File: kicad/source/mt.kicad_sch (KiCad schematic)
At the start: 18 parts, among them IC1 MSPM0G3507SPMR, IC2 DAC082S085CIMMX_NOPB, IC3 IS62WV1288BLL-55QLI, IC4 MCP73831T-2ACI_OT, IC5 RT9167A-33GB, IC6 SN74HC148NSR, IC7 TLV9152IDR, IC8 TPS613222ADBVR, IC9 BQ29728DSER, J1 694106301002, J2 SJ1-3524N, Q1 CSD16406Q3, Q2 CSD16406Q3, U1 1043

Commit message: completed power electronics schematic
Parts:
- removed VR2: PTV09A-4020F-C103, PTV09A-4020F-C103:PTV09A4020FC103, symbol PTV09A-4020F-C103:PTV09A-4020F-C103
- added C1, C2, C4, C7: 4.7u, Capacitor_SMD:C_0402_1005Metric, symbol Device:C
- added C3, C8: 0.1u, Capacitor_SMD:C_0402_1005Metric, symbol Device:C
- added C5, C6: 22u, Capacitor_SMD:C_0603_1608Metric, symbol Device:C
- added D1: LED, LED_THT:LED_D5.0mm, symbol Device:LED
- added J3: Conn_01x05_MountingPin, Connector_PinHeader_2.54mm:PinHeader_1x05_P2.54mm_Horizontal, symbol Connector_Generic_MountingPin:Conn_01x05_MountingPin
- added L1: 2.2u, Inductor_SMD:L_1008_2520Metric, symbol Device:L
- added R1: 4.7k, Resistor_SMD:R_0402_1005Metric, symbol Device:R_US
- added R2: 2k, Resistor_SMD:R_0402_1005Metric, symbol Device:R_US
- added R3: 2.2k, Resistor_SMD:R_0402_1005Metric, symbol Device:R_US
- added R4: 330, Resistor_SMD:R_0402_1005Metric, symbol Device:R_US
- added VR2: PTV112-4420A-C104, PTV1124420AC104, symbol PTV112-4420A-C104:PTV112-4420A-C104
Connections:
- net GND: now reaches Q1.1 (S_1), Q1.2 (S_2), Q1.3 (S_3)
- net GND: now also IC4.2 (VSS), IC5.2 (GND), IC8.2 (GND), J1.2 (GND_1), J1.3 (GND_2), C1.2, C2.2, C4.2, C5.2, C6.2, C7.2, C8.2, R2.2, R3.1
- net at Q1.4 (G): now also IC9.2 (COUT)
- net at Q1.5 (D_1), Q1.6 (D_2), Q1.7 (D_3)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: now also Q2.5 (D_1), Q2.6 (D_2), Q2.7 (D_3), Q2.8 (D_4)
- net at IC8.1 (SW): now also L1.1
- net at IC8.4 (VOUT): now also IC5.1 (VIN), IC5.3 (EN), C5.1, C6.1
- net at IC9.3 (DOUT): now also Q2.4 (G)
- net at IC9.4 (VSS): now also Q2.1 (S_1), Q2.2 (S_2), Q2.3 (S_3), U1.2 (-), C3.2
- net at IC9.5 (BAT): now also C3.1, R4.2
- net at IC9.6 (V-): now also R3.2
- net at J1.1 (POWER): now also IC4.4 (VDD), C1.1, D1.2 (A)
- net VBAT: now reaches S1.2
- net VBAT: now also C4.1, L1.2
- net CELL+: now reaches S1.3
- net CELL+: now also IC4.3 (VBAT), U1.1 (+), C2.1, R4.1
- net at IC4.1 (STAT): now also R1.2
- net at IC4.5 (PROG): now also R2.1
- net at IC5.4 (BP): now also C8.1
- net at IC5.5 (VOUT): now also C7.1
- net at S2.1: now also S2.2
- net at S2.3: now also S2.4
- new net: D1.1 (K), R1.1
- no-connect marks 5 -> 9
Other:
- note added: "Charging"
- note added: "Power"
- note added: "Protection"
- note added: "Regulation"
- note added: "TODO: add all JLCPCB part # to ICs!"
- moved on the sheet: IC4, IC5, IC8, IC9, J1, Q1, Q2, S1, U1

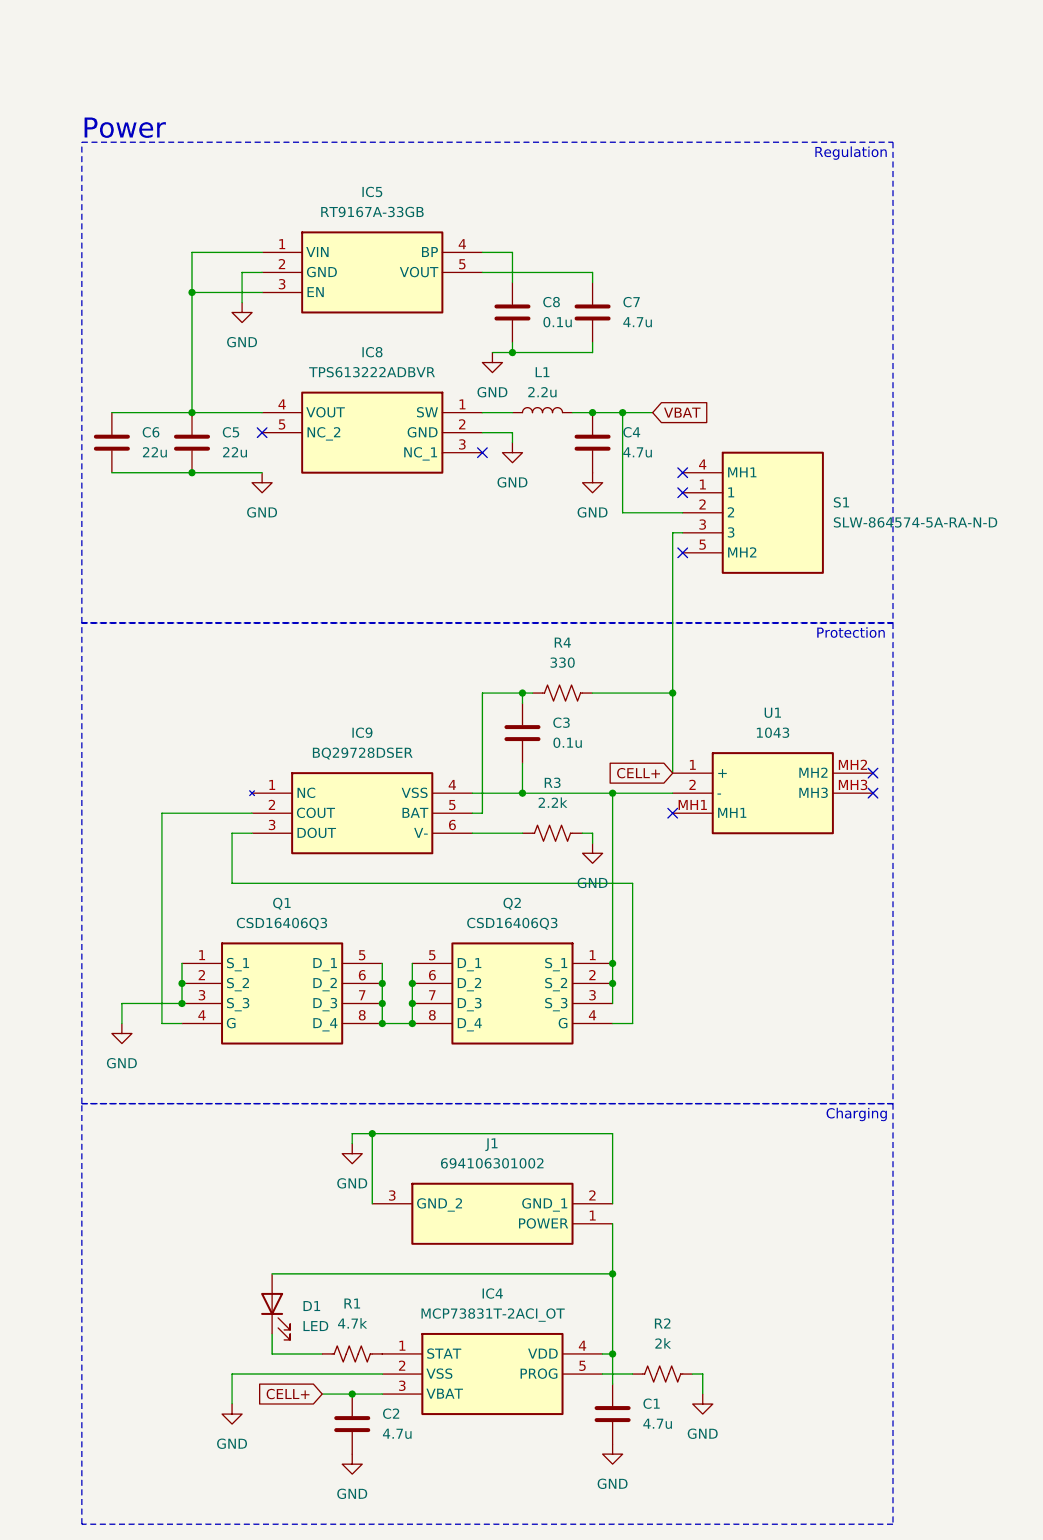
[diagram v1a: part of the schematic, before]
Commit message: revised power electronics caps, added JLCPCB part numbers to SMD power electronics
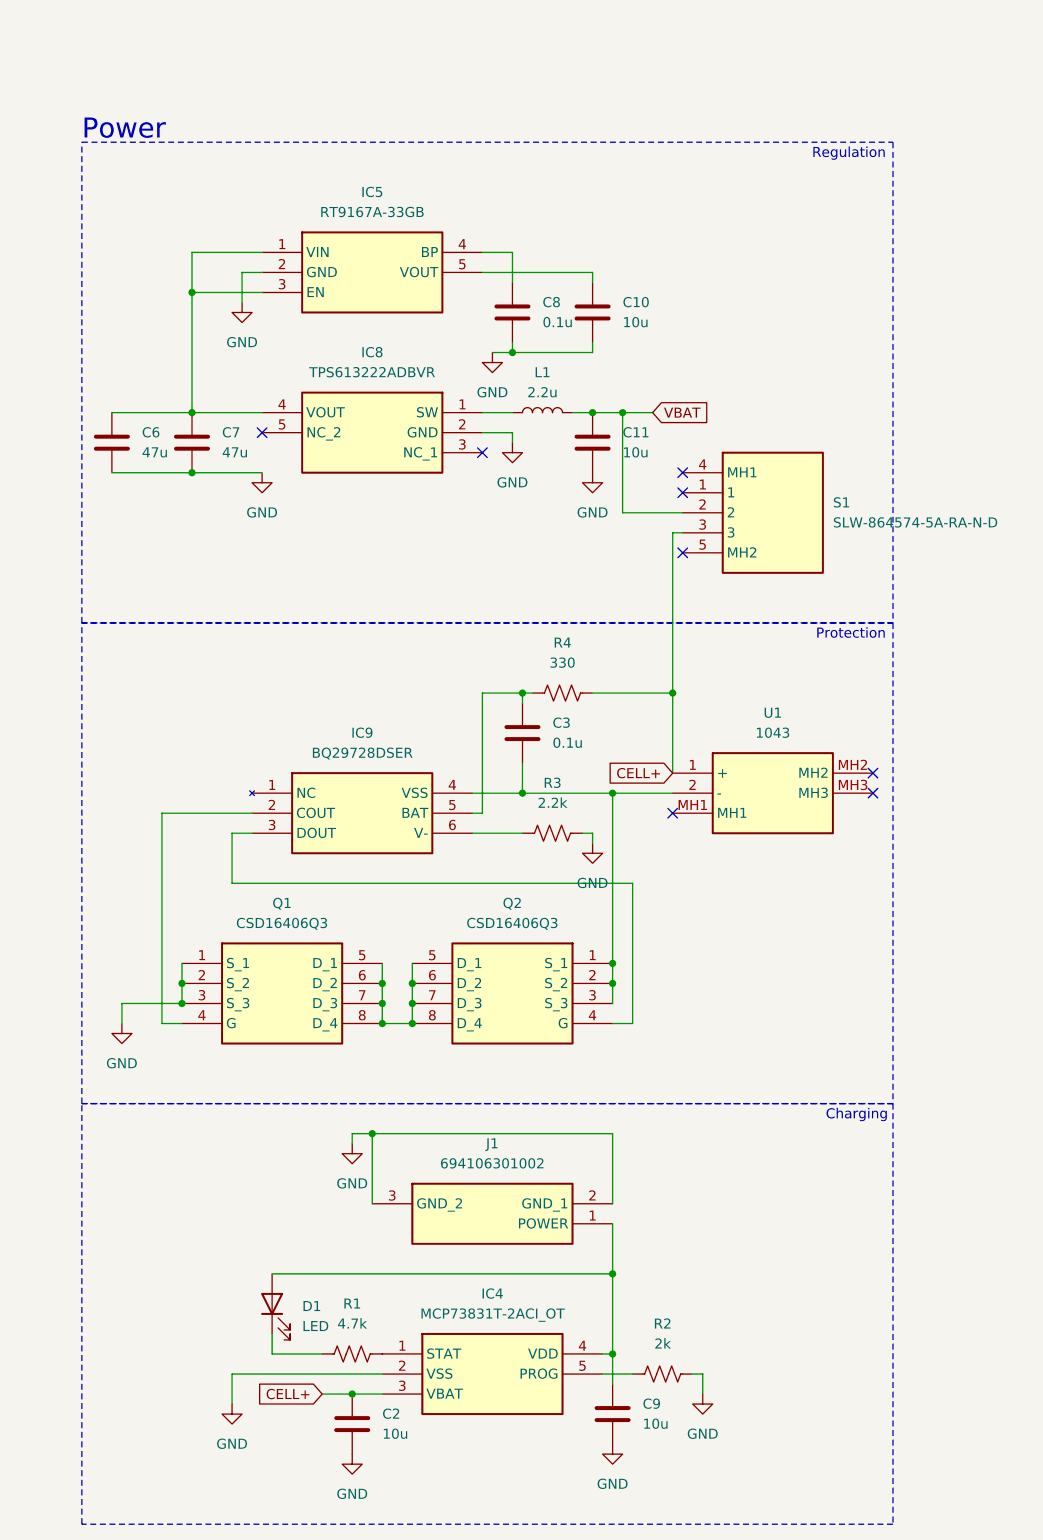
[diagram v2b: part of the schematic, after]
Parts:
- removed C1, C4: 4.7u, Capacitor_SMD:C_0402_1005Metric, symbol Device:C
- removed C5: 22u, Capacitor_SMD:C_0603_1608Metric, symbol Device:C
- added C10, C11, C9: 10u, Capacitor_SMD:C_0603_1608Metric, symbol Device:C
- C2: value 4.7u -> 10u; footprint Capacitor_SMD:C_0402_1005Metric -> Capacitor_SMD:C_0603_1608Metric; JLCPCB C23733 -> C19702
- C3, C8: footprint Capacitor_SMD:C_0402_1005Metric -> Capacitor_SMD:C_1206_3216Metric; JLCPCB C1525 -> C97946
- C6: value 22u -> 47u; footprint Capacitor_SMD:C_0603_1608Metric -> Capacitor_SMD:C_0805_2012Metric; JLCPCB C59461 -> C16780
- C7: value 4.7u -> 47u; footprint Capacitor_SMD:C_0402_1005Metric -> Capacitor_SMD:C_0805_2012Metric; JLCPCB C23733 -> C16780
- IC4: JLCPCB (none) -> C424093
- IC5: JLCPCB (none) -> C113513
- IC8: JLCPCB (none) -> C2071163
- IC9: JLCPCB (none) -> C3682679
- Q1, Q2: JLCPCB (none) -> C2861720
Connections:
- net GND: now also C10.2, C11.2, C9.2
- net VBAT: now also C11.1
- net at C7.1: now also C6.1, IC5.1 (VIN), IC5.3 (EN), IC8.4 (VOUT); no longer IC5.5 (VOUT)
- net at D1.2 (A), IC4.4 (VDD), J1.1 (POWER): now also C9.1
- new net: C10.1, IC5.5 (VOUT)

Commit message: completed audio electronics schematic
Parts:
- added C10, C9: 4.7n, Capacitor_SMD:C_0402_1005Metric, symbol Device:C
- added C11: 10u, Capacitor_SMD:C_0603_1608Metric, symbol Device:C
- added C12, C13: 100n, Capacitor_SMD:C_1206_3216Metric, symbol Device:C
- added J4: Conn_01x09_MountingPin, Connector_PinHeader_2.54mm:PinHeader_1x09_P2.54mm_Vertical, symbol Connector_Generic_MountingPin:Conn_01x09_MountingPin
- added R10, R9: 100k, Resistor_SMD:R_0402_1005Metric, symbol Device:R_US
- added R5, R6, R7, R8: 10k, Resistor_SMD:R_0402_1005Metric, symbol Device:R_US
- C3: value 0.1u -> 100n
- C7: renamed from C8; value 0.1u -> 100n
- IC7: JLCPCB (none) -> C882649
- L1: JLCPCB C86092 -> C86092
- R2: JLCPCB C4109 -> C4109
- R3: JLCPCB C25879 -> C25879
- R4: JLCPCB C25104 -> C25104
- renumbered C2 to C1, C9 to C2, C11 to C4, C7 to C5, C10 to C8
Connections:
- net GND: now also IC7.4 (V-), J2.1 (SLEEVE), VR1.R32 (WIPER_3), VR1.R42 (WIPER_4), C10.2, C11.2, C9.2, R10.2, R9.2
- net L: now reaches IC7.1 (OUT1)
- net L: now also VR1.R12 (WIPER_1), C12.1
- net RV1A: now reaches IC7.2 (IN1-)
- net RV1A: now also VR1.R11 (CCW_1), R5.1
- net RV3A: now reaches IC7.3 (IN1+)
- net RV3A: now also VR1.R31 (CCW_3), R7.2
- net RV4A: now reaches IC7.5 (IN2+)
- net RV4A: now also VR1.R41 (CCW_4), R8.1
- net RV2A: now reaches IC7.6 (IN2-)
- net RV2A: now also VR1.R21 (CCW_2), R6.2
- net R: now reaches IC7.7 (OUT2)
- net R: now also VR1.R22 (WIPER_2), C13.1
- net VDD: now reaches IC7.8 (V+)
- net VDD: now also C8.1, IC5.5 (VOUT), C11.1, R7.1, R8.2
- net DACL: now reaches IC2.2 (VOUTA)
- net DACL: now also VR2.A1
- net DACR: now reaches IC2.3 (VOUTB)
- net DACR: now also VR2.B2
- net at J2.2 (TIP): now also C12.2, R9.1
- net at J2.3 (RING): now also C13.2, R10.1
- net at VR2.A2: now also C9.1, R5.2
- net at VR2.B1: now also C10.1, R6.1
- no-connect marks 9 -> 22
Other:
- note added: "Amplifier"
- note added: "Audio"
- note added: "Highpass/Output"
- note added: "Lowpass"
- note added: "Remember to add JLCPCB part #s to all SMD parts!"
- note removed: "TODO: add all JLCPCB part # to ICs!"
- moved on the sheet: C2, D1, IC1, IC2, IC3, IC6, IC7, J2, J3, R2, S2, VR1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

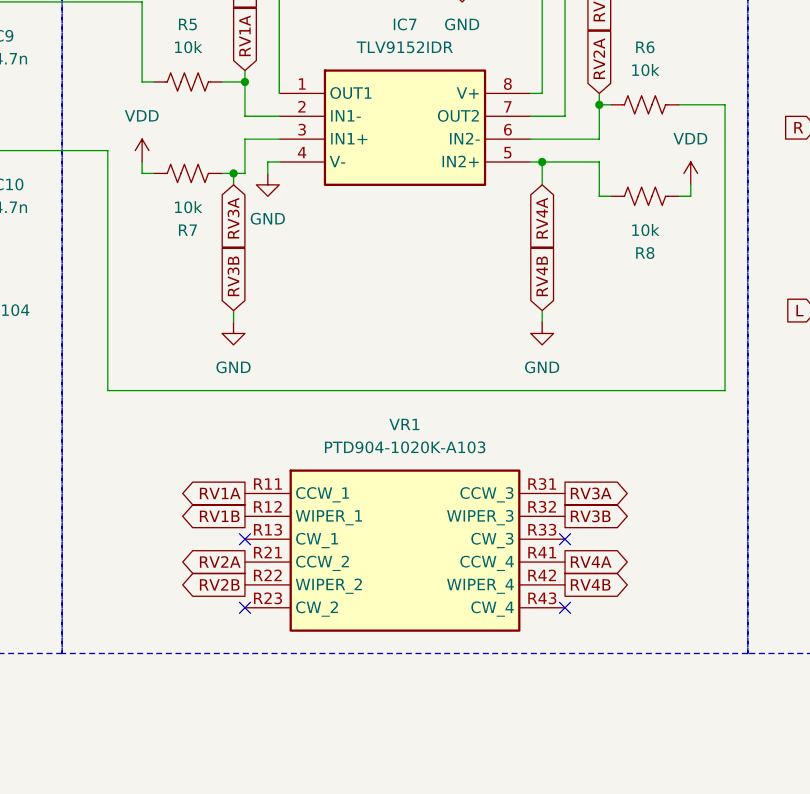
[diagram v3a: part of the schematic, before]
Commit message: revised audio electronics volume pot
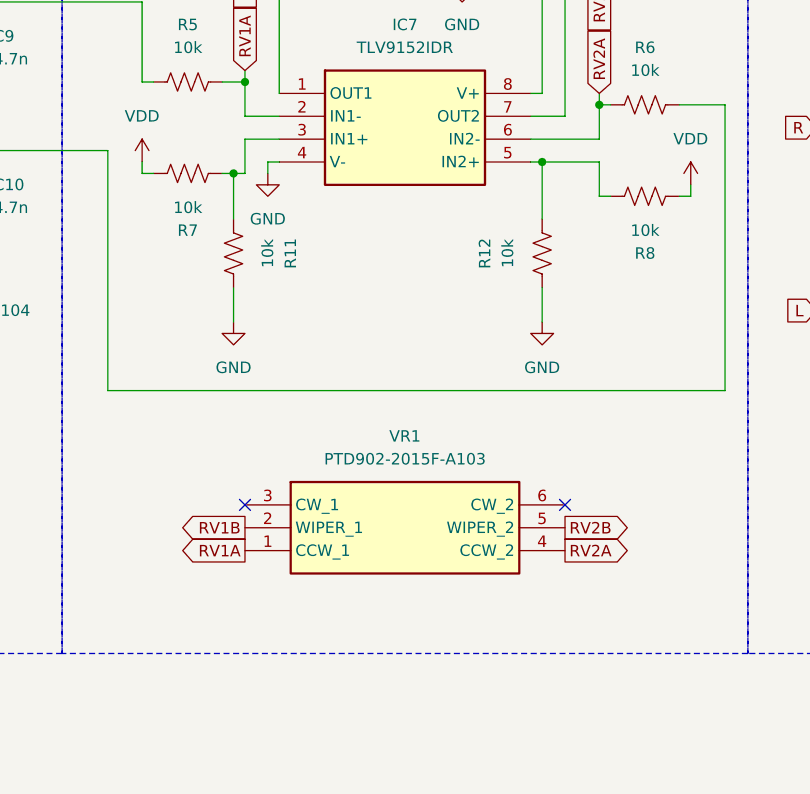
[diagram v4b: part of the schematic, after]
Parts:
- removed VR1: PTD904-1020K-A103, PTD904-1020K-A103:PTD9041020KA103, symbol PTD904-1020K-A103:PTD904-1020K-A103
- added R11, R12: 10k, Resistor_SMD:R_0402_1005Metric, symbol Device:R_US
- added VR1: PTD902-2015F-A103, PTD9022015FA103, symbol PTD902-2015F-A103:PTD902-2015F-A103
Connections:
- net GND: now also R11.1, R12.2
- net L: now also VR1.2 (WIPER_1)
- net R: now also VR1.5 (WIPER_2)
- net RV1A: now also VR1.1 (CCW_1)
- net RV2A: now also VR1.4 (CCW_2)
- net RV3A: no longer names the net of IC7.3 (IN1+), R7.2
- net RV3A: now also R11.2
- net RV4A: no longer names the net of IC7.5 (IN2+), R8.1
- net RV4A: now also R12.1
- no-connect marks 22 -> 20
